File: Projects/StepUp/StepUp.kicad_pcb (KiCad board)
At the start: 4 copper layers, 136 parts, among them J1 USB_C_Receptacle_USB2.0_16P, J10 Conn_01x02, J11 Conn_02x03_Counter_Clockwise, J2 Conn_01x02, J3 Conn_02x03_Counter_Clockwise, J4 Conn_02x06_Counter_Clockwise, J5 TBLH10-350-04BK, J6 Conn_01x02, J7 Conn_01x02, J8 Conn_01x02, J9 Conn_01x02, Q1 BSS84, Q2 2N7002, Q3 BSS83P, Q4 BSS83P, SW1 SW_Push, SW2 SW_Push, SW3 SW_Push, U1 USBLC6-2SC6, U2 W25Q128JVS, U3 RP2040, U4 TMC2300-LA, U5 MCP73832T-2ACI_OT, U6 NCP1117-3.3_SOT223, U7 MIC2253, Y1 ABM8-272-T3

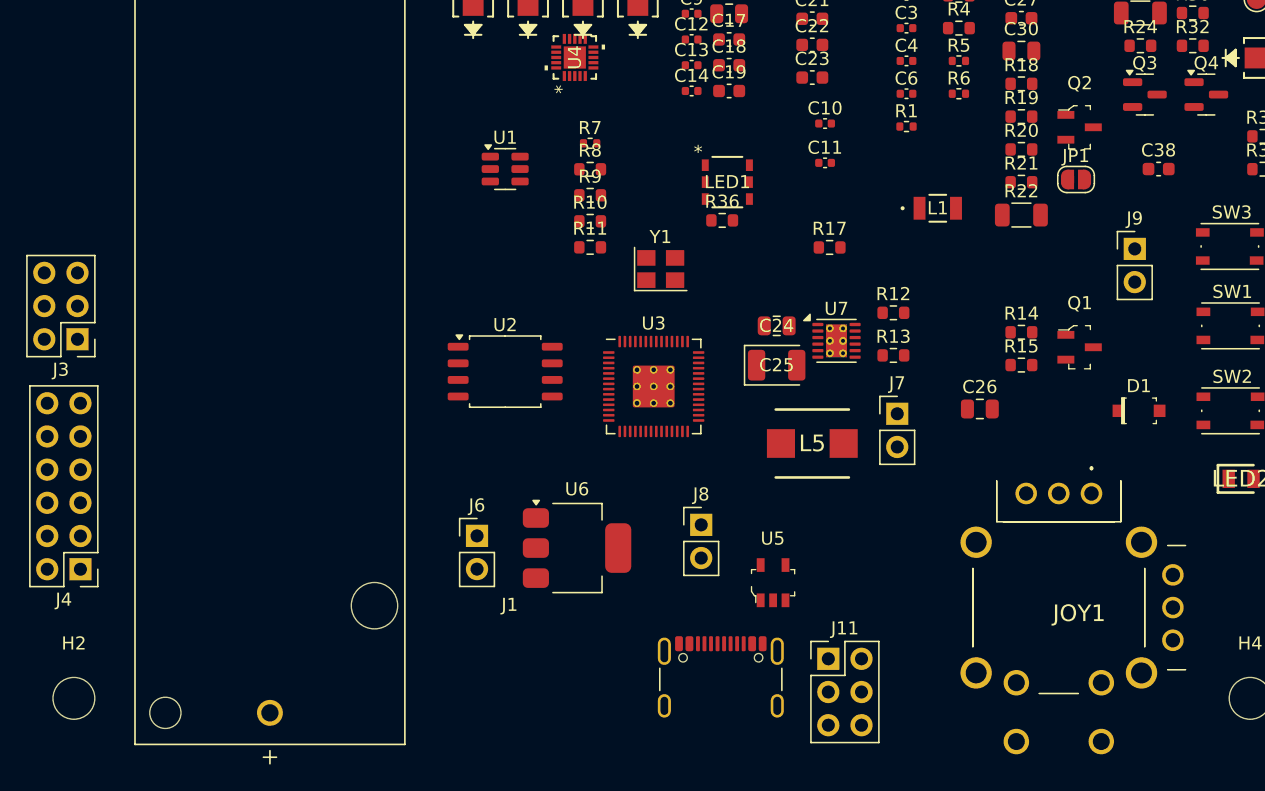
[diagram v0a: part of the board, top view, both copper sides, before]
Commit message: chore(pins): MCU_BOOST_EN to MCU, fixed errors
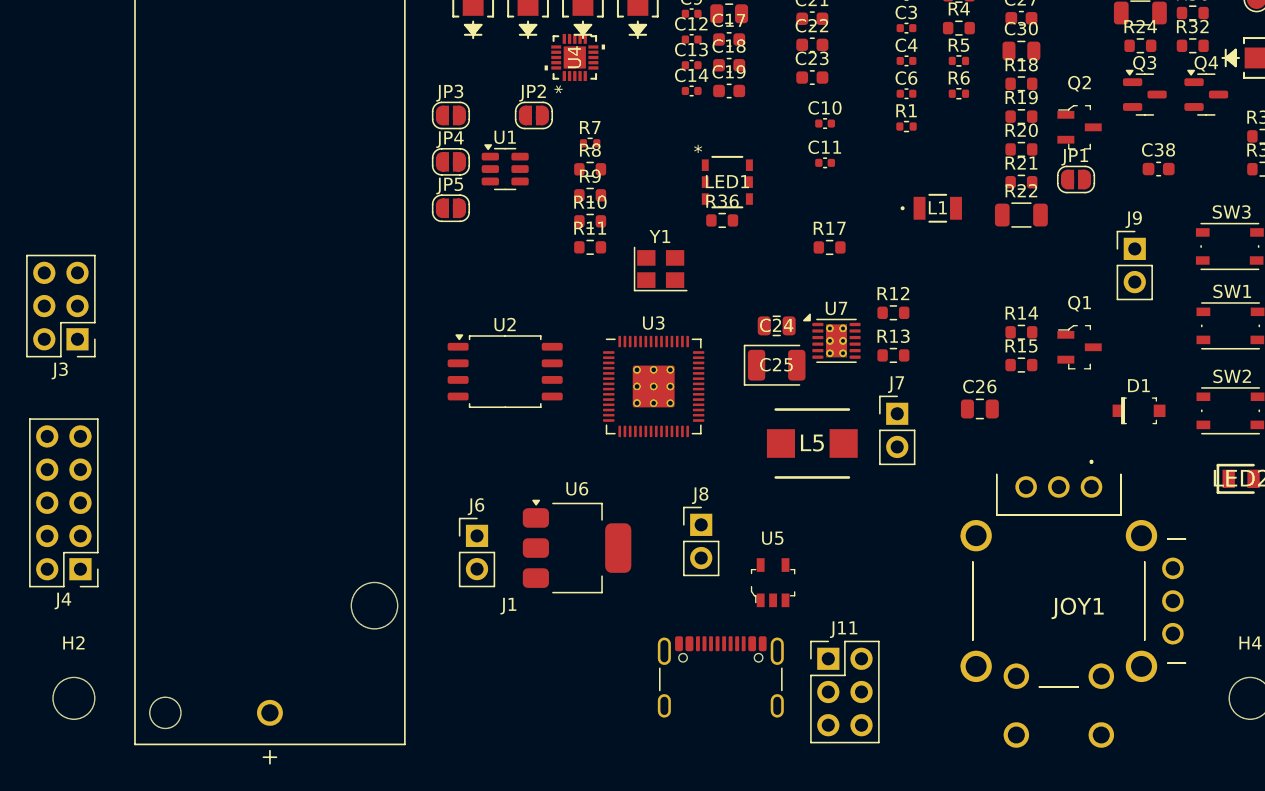
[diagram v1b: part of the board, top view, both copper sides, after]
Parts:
- added JP2: SolderJumper_2_Open, Jumper:SolderJumper-2_P1.3mm_Open_RoundedPad1.0x1.5mm, F.Cu at (125.2, 95.4)
- added JP3: SolderJumper_2_Open, Jumper:SolderJumper-2_P1.3mm_Open_RoundedPad1.0x1.5mm, F.Cu at (118.8, 95.4)
- added JP4: SolderJumper_2_Open, Jumper:SolderJumper-2_P1.3mm_Open_RoundedPad1.0x1.5mm, F.Cu at (118.8, 99.0)
- added JP5: SolderJumper_2_Open, Jumper:SolderJumper-2_P1.3mm_Open_RoundedPad1.0x1.5mm, F.Cu at (118.8, 102.5)
- J4: value Conn_02x06_Counter_Clockwise -> Conn_02x05_Counter_Clockwise; footprint Connector_PinHeader_2.54mm:PinHeader_2x06_P2.54mm_Vertical -> Connector_PinHeader_2.54mm:PinHeader_2x05_P2.54mm_Vertical
- moved JOY1 0.50 mm to (167.9, 123.8)
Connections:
- C35 pad 2: Vbat_monitor -> Net-(JP3-B)
- C36 pad 2: Vmotor_monitor -> Net-(JP4-B)
- C37 pad 2: VUSB_monitor -> Net-(JP5-B)
- J4 pad 10: /MCU/GPIO18 -> /MCU/GPIO10
- J4 pad 5: /MCU/GPIO10 -> /MCU/GPIO16
- J4 pad 6: /MCU/GPIO11 -> /MCU/GPIO17
- J4 pad 9: /MCU/GPIO19 -> /MCU/GPIO11
- JOY1 pad 12: JOYSTSICK_AXIS_H -> JOYSTSICK_AXIS_V
- JOY1 pad 2: JOYSTSICK_AXIS_V -> JOYSTSICK_AXIS_H
- JP1 pad 2: /Power/MCU_BOOST_EN -> MCU_BOOST_EN
- Q4 pad 3: /Power/MCU_BOOST_EN -> MCU_BOOST_EN
- R36 pad 1: Vbat_monitor -> Net-(JP3-B)
- R37 pad 2: Vbat_monitor -> Net-(JP3-B)
- R38 pad 1: Vmotor_monitor -> Net-(JP4-B)
- R39 pad 1: Vmotor_monitor -> Net-(JP4-B)
- R41 pad 1: VUSB_monitor -> Net-(JP5-B)
- R42 pad 2: VUSB_monitor -> Net-(JP5-B)
- SW3 pad 2: /MCU/GPIO13 -> Net-(JP2-B)
- U3 pad 29: /MCU/GPIO18 -> VUSB_MONITOR
- U3 pad 30: /MCU/GPIO19 -> MCU_BOOST_EN
- U3 pad 32: VUSB_monitor -> VUSB_MONITOR
- U3 pad 40: Vbat_monitor -> VBAT_MONITOR
- U3 pad 41: Vmotor_monitor -> VMOTOR_MONITOR

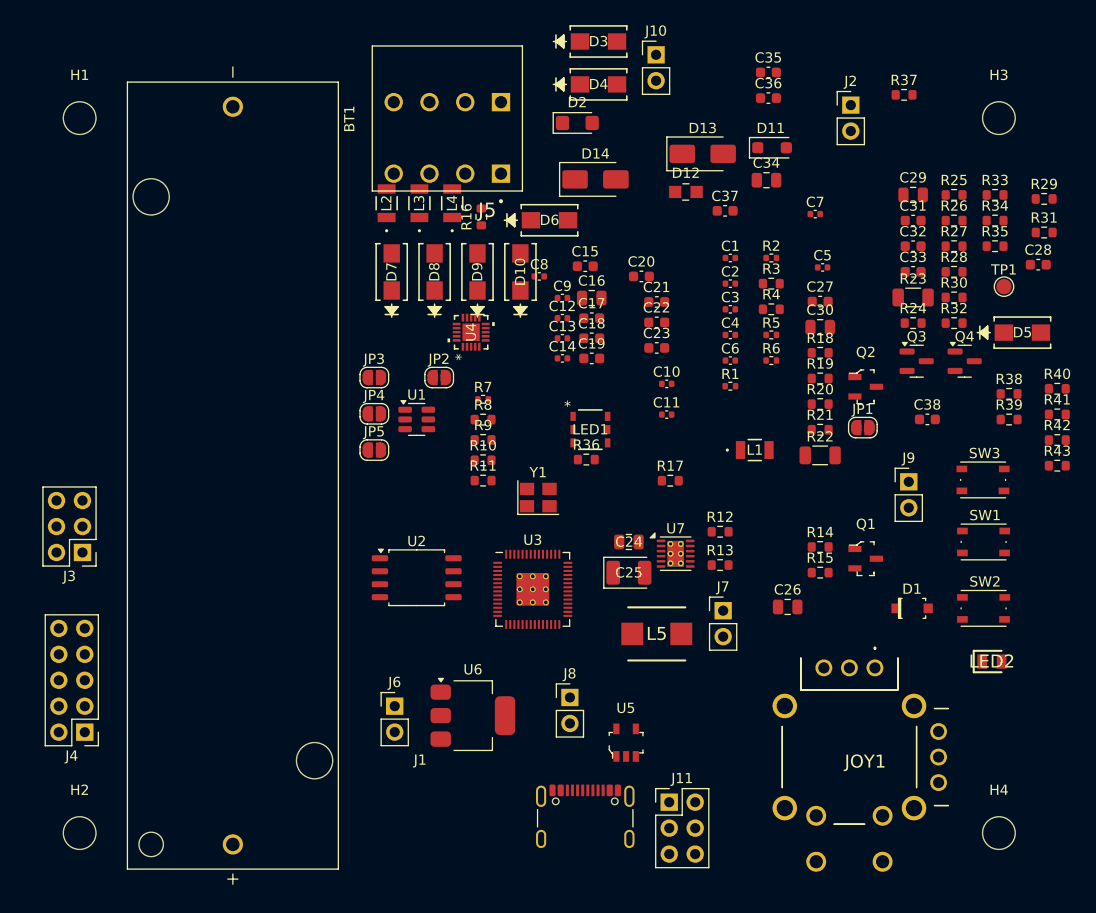
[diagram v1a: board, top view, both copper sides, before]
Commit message: feat(layout): Blocks organised
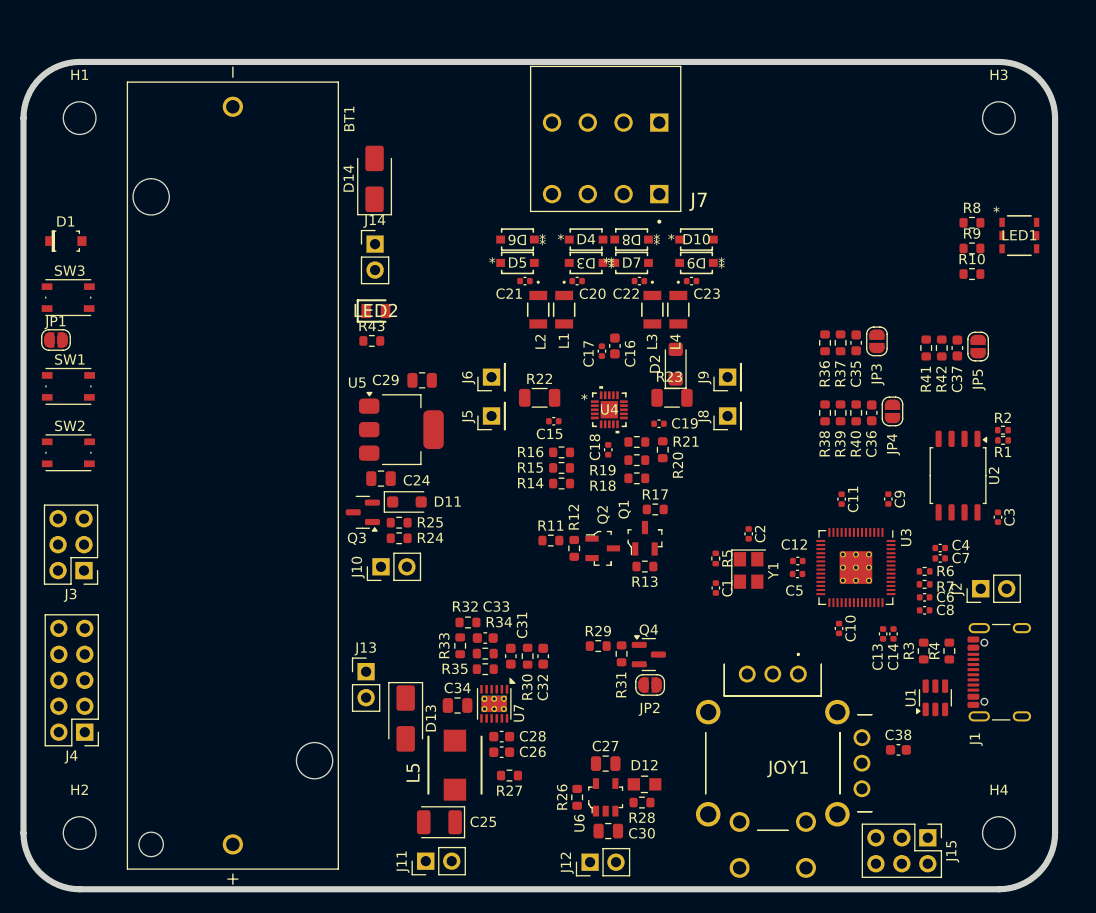
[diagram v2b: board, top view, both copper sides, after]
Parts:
- removed TP1: TestPoint, TestPoint:TestPoint_Pad_D1.5mm
- added J12: Conn_01x02, Connector_PinHeader_2.54mm:PinHeader_1x02_P2.54mm_Vertical, F.Cu at (140.0, 142.8)
- added J13: Conn_01x02, Connector_PinHeader_2.54mm:PinHeader_1x02_P2.54mm_Vertical, F.Cu at (118.0, 124.2)
- added J14: Conn_01x02, Connector_PinHeader_2.54mm:PinHeader_1x02_P2.54mm_Vertical, F.Cu at (118.9, 82.3)
- added J15: Conn_02x03_Counter_Clockwise, Connector_PinHeader_2.54mm:PinHeader_2x03_P2.54mm_Vertical, F.Cu at (173.0, 140.5)
- C15, C17, C18, C19, C20, C21, C22, C23: footprint Capacitor_SMD:C_0603_1608Metric -> Capacitor_SMD:C_0402_1005Metric
- C16: footprint Capacitor_SMD:C_0805_2012Metric -> Capacitor_SMD:C_0603_1608Metric
- C26: value 4.7u -> 2.2uF; footprint Capacitor_SMD:C_0805_2012Metric -> Capacitor_SMD:C_0603_1608Metric
- C27: value 2.2uF -> 4.7u; footprint Capacitor_SMD:C_0603_1608Metric -> Capacitor_SMD:C_0805_2012Metric
- C29: value 4.7u -> 10uF
- C30: value 10uF -> 4.7u
- D10, D3, D4, D5, D6, D7, D8, D9: value SSA33L-E3/61T -> B5819W-TP; footprint Snapeda:DIODE_DO214AC -> Snapeda:SDO_SOD-123_MCC
- J11: value Conn_02x03_Counter_Clockwise -> Conn_01x02; footprint Connector_PinHeader_2.54mm:PinHeader_2x03_P2.54mm_Vertical -> Connector_PinHeader_2.54mm:PinHeader_1x02_P2.54mm_Vertical
- J5: value TBLH10-350-04BK -> Conn_01x01_Pin; footprint Snapeda:CUI_TBLH10-350-04BK -> Connector_PinHeader_2.54mm:PinHeader_1x01_P2.54mm_Vertical
- J6, J8, J9: value Conn_01x02 -> Conn_01x01_Pin; footprint Connector_PinHeader_2.54mm:PinHeader_1x02_P2.54mm_Vertical -> Connector_PinHeader_2.54mm:PinHeader_1x01_P2.54mm_Vertical
- J7: value Conn_01x02 -> TBLH10-350-04BK; footprint Connector_PinHeader_2.54mm:PinHeader_1x02_P2.54mm_Vertical -> Snapeda:CUI_TBLH10-350-04BK
- R26: value 510R -> 2kR
- R27: value 620R -> 100kR
- R28: value 100kR -> 620R
- R29: value 620R -> 100R
- R30: value 100R -> 620R
- R31: value 9.09kR -> 100kR
- R32: value 10kR -> 9.09kR
- R33: value 100kR -> 10kR
- U5: value MCP73832T-2ACI_OT -> NCP1117-3.3_SOT223; footprint digikey-footprints:SOT-753 -> Package_TO_SOT_SMD:SOT-223-3_TabPin2
- U6: value NCP1117-3.3_SOT223 -> MCP73832T-2ACI_OT; footprint Package_TO_SOT_SMD:SOT-223-3_TabPin2 -> digikey-footprints:SOT-753
- moved SW3 91.3 mm to (88.9, 87.6)
- moved SW1 90.9 mm to (88.9, 96.3)
- moved SW2 90.9 mm to (88.9, 102.8)
- moved D1 90.3 mm to (88.6, 82.0)
- moved JP1 79.5 mm to (87.7, 91.7)
- moved C28 70.0 mm to (131.3, 130.6)
- moved LED2 69.4 mm to (119.0, 88.9)
- moved R33 68.5 mm to (127.3, 121.7), turned to 90 degrees
- moved R43 68.2 mm to (118.6, 91.8)
- moved R27 67.7 mm to (132.1, 134.4), turned to 180 degrees
- moved R26 67.5 mm to (138.7, 136.5), turned to 90 degrees
- moved R34 65.5 mm to (129.7, 122.4), turned to 180 degrees
- moved R35 64.9 mm to (129.7, 124.0)
- moved R25 63.1 mm to (121.3, 109.6), turned to 180 degrees
- moved D13 62.5 mm to (121.9, 128.8), turned to -90 degrees
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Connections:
- net /Motor Driver/VCC_IO renamed /Motor Driver/TMC_VCC_IO
- C26 pad 1: GND -> /Power/BOOST_VIN
- C26 pad 2: V_USB -> GND
- C27 pad 1: /Power/BOOST_VIN -> GND
- C27 pad 2: GND -> V_USB
- C29 pad 1: Net-(J8-Pin_2) -> +3V3
- C30 pad 1: +3V3 -> Net-(J12-Pin_2)
- C35 pad 2: Net-(JP3-B) -> Net-(JP3-A)
- C36 pad 2: Net-(JP4-B) -> Net-(JP4-A)
- C37 pad 2: Net-(JP5-B) -> Net-(JP5-A)
- J10 pad 1: Vbat -> V_USB
- J10 pad 2: Net-(D14-K) -> Net-(D11-A)
- J11 pad 1: JOYSTSICK_AXIS_V -> Vbat
- J11 pad 2: JOYSTSICK_AXIS_H -> /Power/BOOST_VIN
- J6 pad 1: V_USB -> GND
- J8 pad 1: Vbat -> /Motor Driver/BRB
- J9 pad 1: VMotor -> GND
- JP1 pad 1: /Power/BOOST_ENABLE -> /MCU/GPIO13
- JP1 pad 2: MCU_BOOST_EN -> Net-(JP1-B)
- JP2 pad 1: /MCU/GPIO13 -> /Power/BOOST_ENABLE
- JP2 pad 2: Net-(JP2-B) -> MCU_BOOST_EN
- JP3 pad 1: VBAT_MONITOR -> Net-(JP3-A)
- JP3 pad 2: Net-(JP3-B) -> VBAT_MONITOR
- JP4 pad 1: VMOTOR_MONITOR -> Net-(JP4-A)
- JP4 pad 2: Net-(JP4-B) -> VMOTOR_MONITOR
- JP5 pad 1: VUSB_MONITOR -> Net-(JP5-A)
- JP5 pad 2: Net-(JP5-B) -> VUSB_MONITOR
- R22 pad 2: Net-(U4-BRA) -> /Motor Driver/BRA
- R23 pad 2: Net-(U4-BRB) -> /Motor Driver/BRB
- R26 pad 2: Net-(U5-PROG) -> Net-(U6-PROG)
- R27 pad 1: Net-(U5-STAT) -> GND
- R27 pad 2: Net-(D12-Pad2) -> /Power/BOOST_ENABLE
- R28 pad 1: GND -> Net-(U6-STAT)
- R28 pad 2: /Power/BOOST_ENABLE -> Net-(D12-Pad2)
- R29 pad 1: Net-(U7-COMP) -> V_USB
- R29 pad 2: Net-(C32-Pad1) -> Net-(Q4-G)
- R30 pad 1: V_USB -> Net-(U7-COMP)
- R30 pad 2: Net-(Q4-G) -> Net-(C32-Pad1)
- R31 pad 1: Net-(U7-OVP) -> GND
- R31 pad 2: /Power/BOOST_VOUT -> Net-(Q4-G)
- R32 pad 1: GND -> Net-(U7-OVP)
- R32 pad 2: Net-(U7-OVP) -> /Power/BOOST_VOUT
- R33 pad 2: Net-(Q4-G) -> Net-(U7-OVP)
- R36 pad 1: Net-(JP3-B) -> Net-(JP3-A)
- R37 pad 2: Net-(JP3-B) -> Net-(JP3-A)
- R38 pad 1: Net-(JP4-B) -> Net-(JP4-A)
- R39 pad 1: Net-(JP4-B) -> Net-(JP4-A)
- R41 pad 1: Net-(JP5-B) -> Net-(JP5-A)
- R42 pad 2: Net-(JP5-B) -> Net-(JP5-A)
- SW3 pad 2: Net-(JP2-B) -> Net-(JP1-B)
- U4 pad 16: Net-(U4-BRB) -> /Motor Driver/BRB
- U4 pad 20: Net-(U4-BRA) -> /Motor Driver/BRA
- U5 pad 1: Net-(U5-STAT) -> GND
- U5 pad 2: GND -> +3V3
- U5 pad 3: Net-(J8-Pin_2) -> Net-(D11-K)
- U6 pad 1: GND -> Net-(U6-STAT)
- U6 pad 2: +3V3 -> GND
- U6 pad 3: Net-(D11-K) -> Net-(J12-Pin_2)
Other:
- board outline added: 101 x 81 mm
